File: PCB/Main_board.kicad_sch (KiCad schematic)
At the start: 296 parts, among them J1 USB_C_Receptacle_USB2.0_14P, J2 Conn_02x03_Odd_Even, SW1 SW_Push, SW10 SW_Push, SW11 SW_Push, SW12 SW_Push, SW13 SW_Push, SW14 SW_Push, SW15 SW_Push, SW16 SW_Push, SW17 SW_Push, SW18 SW_Push, SW19 SW_Push, SW2 SW_Push, SW20 SW_Push, SW21 SW_Push, SW22 SW_Push, SW23 SW_Push, SW24 SW_Push, SW25 SW_Push, SW26 SW_Push, SW27 SW_Push, SW28 SW_Push, SW29 SW_Push, SW3 SW_Push, SW30 SW_Push, SW31 SW_Push, SW32 SW_Push, SW33 SW_Push, SW34 SW_Push, SW35 SW_Push, SW36 SW_Push, SW37 SW_Push, SW38 SW_Push, SW39 SW_Push, SW4 SW_Push, SW40 SW_Push, SW41 SW_Push, SW42 SW_Push, SW43 SW_Push, SW44 SW_Push, SW45 SW_Push, SW46 SW_Push, SW47 SW_Push, SW48 SW_Push, SW49 SW_Push, SW5 SW_Push, SW50 SW_Push, SW51 SW_Push, SW52 SW_Push, SW53 SW_Push, SW54 SW_Push, SW55 SW_Push, SW56 SW_Push, SW57 SW_Push, SW58 SW_Push, SW59 SW_Push, SW6 SW_Push, SW60 SW_Push, SW61 SW_Push, SW62 SW_Push, SW63 SW_Push, SW64 SW_Push, SW65 SW_Push, SW66 SW_Push, SW67 SW_Push, SW68 SW_Push, SW69 SW_Push, SW7 SW_Push, SW70 SW_Push, SW71 SW_Push, SW72 SW_Push, SW73 SW_Push, SW74 SW_Push, SW75 SW_Push, SW76 SW_Push, SW77 SW_Push, SW78 SW_Push, SW79 SW_Push, SW8 SW_Push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

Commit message: Add: Production files
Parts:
- C1, C2, C3, C5: Comment C15850 -> (none); LCSC Part # (none) -> C15850; Link (none) -> https://jlcpcb.com/partdetail/C15850; Name (none) -> Capacitors; Unit Price ($) (none) -> 0.01
- C11: Comment C49678 -> (none); LCSC Part # (none) -> C49678; Link (none) -> https://jlcpcb.com/partdetail/C49678; Unit Price ($) (none) -> 0.01
- C4: Comment C28323 -> (none); LCSC Part # (none) -> C28323; Link (none) -> https://jlcpcb.com/partdetail/C28323; Unit Price ($) (none) -> 0.01
- C6: Comment C377773 -> (none); LCSC Part # (none) -> C377773; Link (none) -> https://jlcpcb.com/partdetail/C377773; Unit Price ($) (none) -> 0.02
- C7, C8: Comment C1779 -> (none); LCSC Part # (none) -> C1779; Link (none) -> https://jlcpcb.com/partdetail/C1779; Unit Price ($) (none) -> 0.01
- Conn1, Conn2, Conn3, Conn4: Link (none) -> https://www.aliexpress.com/item/1005007636554292.html; Name (none) -> 1X6 Magnetic Pogo Pins; Shipping (none) -> $4.65; Unit Price ($) (none) -> 1.84
- D1, D10, D11, D12, D13, D14, D15, D16, D17, D18, D19, D2, D20, D21, D22, D23, D24, D25, D26, D27, D28, D29, D3, D30, D31, D32, D33, D34, D35, D36, D37, D38, D39, D4, D40, D41, D42, D43, D44, D45, D46, D47, D48, D49, D5, D50, D51, D52, D53, D54, D55, D56, D57, D58, D59, D6, D60, D61, D62, D63, D64, D65, D66, D67, D68, D69, D7, D70, D71, D72, D73, D74, D75, D76, D77, D78, D79, D8, D80, D81, D82, D9: Comment C2099 -> (none); LCSC Part # (none) -> C2099; Link (none) -> https://jlcpcb.com/partdetail/C2099; Name (none) -> Diodes; Unit Price ($) (none) -> 0.01
- D104, D105, D106, D107, D108, D109, D110, D111, D112, D113, D114, D115, D116, D117, D118, D119, D120, D121, D122, D123, D124, D125, D126, D127, D128, D129, D130, D131, D132, D133, D134, D135, D136, D137, D138, D139, D140, D141, D142, D143, D144, D145, D146, D147, D148, D149, D150, D151, D152, D153, D154, D155, D156, D157, D158, D159, D160, D161, D162, D163, D164, D165, D166, D167, D168, D169, D170, D171, D172, D173, D174, D175, D176, D177, D178, D179, D180, D181, D182, D183, D184, D185: Comment C2890035 -> (none); LCSC Part # (none) -> C2890035; Link (none) -> https://jlcpcb.com/partdetail/C2890035; Name (none) -> SK6805 (LEDs); Unit Price ($) (none) -> 0.10
- D83: Comment C587142 -> (none); LCSC Part # (none) -> C587142; Link (none) -> https://jlcpcb.com/partdetail/C587142; Name (none) -> ESDA5V3L (ESD protector for I2C lines); Unit Price ($) (none) -> 0.04
- J1: Comment C165948 -> (none); LCSC Part # (none) -> C165948; Link (none) -> https://jlcpcb.com/partdetail/C165948; Name (none) -> USB Connector; Unit Price ($) (none) -> 0.18
- J2: Comment C6837603 -> (none); LCSC Part # (none) -> C6837603; Link (none) -> https://jlcpcb.com/partdetail/C6837603; Name (none) -> 2x3 1mm PinHeader (SWD Interface); Unit Price ($) (none) -> 0.03
- R1, R2: Comment C27834 -> (none); LCSC Part # (none) -> C27834; Link (none) -> https://jlcpcb.com/partdetail/C27834; Name (none) -> Resistors; Unit Price ($) (none) -> 0.01
- R10, R9: Comment C17673 -> (none); LCSC Part # (none) -> C17673; Link (none) -> https://jlcpcb.com/partdetail/C17673; Unit Price ($) (none) -> 0.01
- R11: Comment C17604 -> (none); LCSC Part # (none) -> C17604; Link (none) -> https://jlcpcb.com/partdetail/C17604; Unit Price ($) (none) -> 0.01
- R12, R6: Comment C2933502 -> (none); LCSC Part # (none) -> C2933502; Link (none) -> https://jlcpcb.com/partdetail/C2933502; Unit Price ($) (none) -> 0.01
- R13, R7: Comment C26112 -> (none); LCSC Part # (none) -> C26112; Link (none) -> https://jlcpcb.com/partdetail/C26112; Unit Price ($) (none) -> 0.01
- R19: Comment C17571 -> (none); LCSC Part # (none) -> C17571; Link (none) -> https://jlcpcb.com/partdetail/C17571; Unit Price ($) (none) -> 0.01
- R20, R22, R4: Comment C17414 -> (none); LCSC Part # (none) -> C17414; Link (none) -> https://jlcpcb.com/partdetail/C17414; Unit Price ($) (none) -> 0.01
- R21: Comment C4328 -> (none); LCSC Part # (none) -> C4328; Link (none) -> https://jlcpcb.com/partdetail/C4328; Unit Price ($) (none) -> 0.01
- R3: Comment C2933423 -> (none); LCSC Part # (none) -> C2933423; Link (none) -> https://jlcpcb.com/partdetail/C2933423; Unit Price ($) (none) -> 0.01
- R5, R8: Comment C17594 -> (none); LCSC Part # (none) -> C17594; Link (none) -> https://jlcpcb.com/partdetail/C17594; Unit Price ($) (none) -> 0.01
- SW1, SW10, SW11, SW12, SW13, SW14, SW15, SW16, SW17, SW18, SW19, SW2, SW20, SW21, SW22, SW23, SW24, SW25, SW26, SW27, SW28, SW29, SW3, SW30, SW31, SW32, SW33, SW34, SW35, SW36, SW37, SW38, SW39, SW4, SW40, SW41, SW42, SW43, SW44, SW45, SW46, SW47, SW48, SW49, SW5, SW50, SW51, SW52, SW53, SW54, SW55, SW56, SW57, SW58, SW59, SW6, SW60, SW61, SW62, SW63, SW64, SW65, SW66, SW67, SW68, SW69, SW7, SW70, SW71, SW72, SW73, SW74, SW75, SW76, SW77, SW78, SW79, SW8, SW80, SW81, SW82, SW9: Comment C5333465 -> (none); LCSC Part # (none) -> C5333465; Link (none) -> https://jlcpcb.com/partdetail/C5333465; Name (none) -> Keys; Unit Price ($) (none) -> 0.1213; moq (none) -> 73
- U1: Comment C687462 -> (none); LCSC Part # (none) -> C687462; Link (none) -> https://jlcpcb.com/partdetail/C687462; Name (none) -> LTC4217 (Hotswap-controller); Unit Price ($) (none) -> 11.90
- U11: Link (none) -> https://www.aliexpress.com/item/1005008597901992.html; Name (none) -> MT3608_Module (Boost converter/ 3V3 -> 5V); Shipping (none) -> $1.99; Unit Price ($) (none) -> 0.99
- U12: Comment C5167252 -> (none); LCSC Part # (none) -> C5167252; Link (none) -> https://jlcpcb.com/partdetail/C5167252; Name (none) -> Slide switch (1825232-1); Price None -> (none); Unit Price ($) (none) -> 0.84
- U2: Comment C283483 -> (none); LCSC Part # (none) -> C283483; Link (none) -> https://jlcpcb.com/partdetail/C283483; Name (none) -> USB6B1 (ESD protector for USB data lines); Unit Price ($) (none) -> 0.4702; moq (none) -> 19
- U3: Comment C5118826 -> (none); LCSC Part # (none) -> C5118826; Link (none) -> https://jlcpcb.com/partdetail/C5118826; Name (none) -> MDBT50Q-1MV2 (MCU); Unit Price ($) (none) -> 6.9468; moq (none) -> 2
- U4: Comment C95414 -> (none); LCSC Part # (none) -> C95414; Link (none) -> https://jlcpcb.com/partdetail/C95414; Name (none) -> LP2985-33DBVR (Voltage stabilizer/ 5V -> 3V3); Unit Price ($) (none) -> 0.12
- U5: Comment C424093 -> (none); LCSC Part # (none) -> C424093; Link (none) -> https://jlcpcb.com/partdetail/C424093; Name (none) -> MCP73831T-2ACI/OT; Unit Price ($) (none) -> 0.72

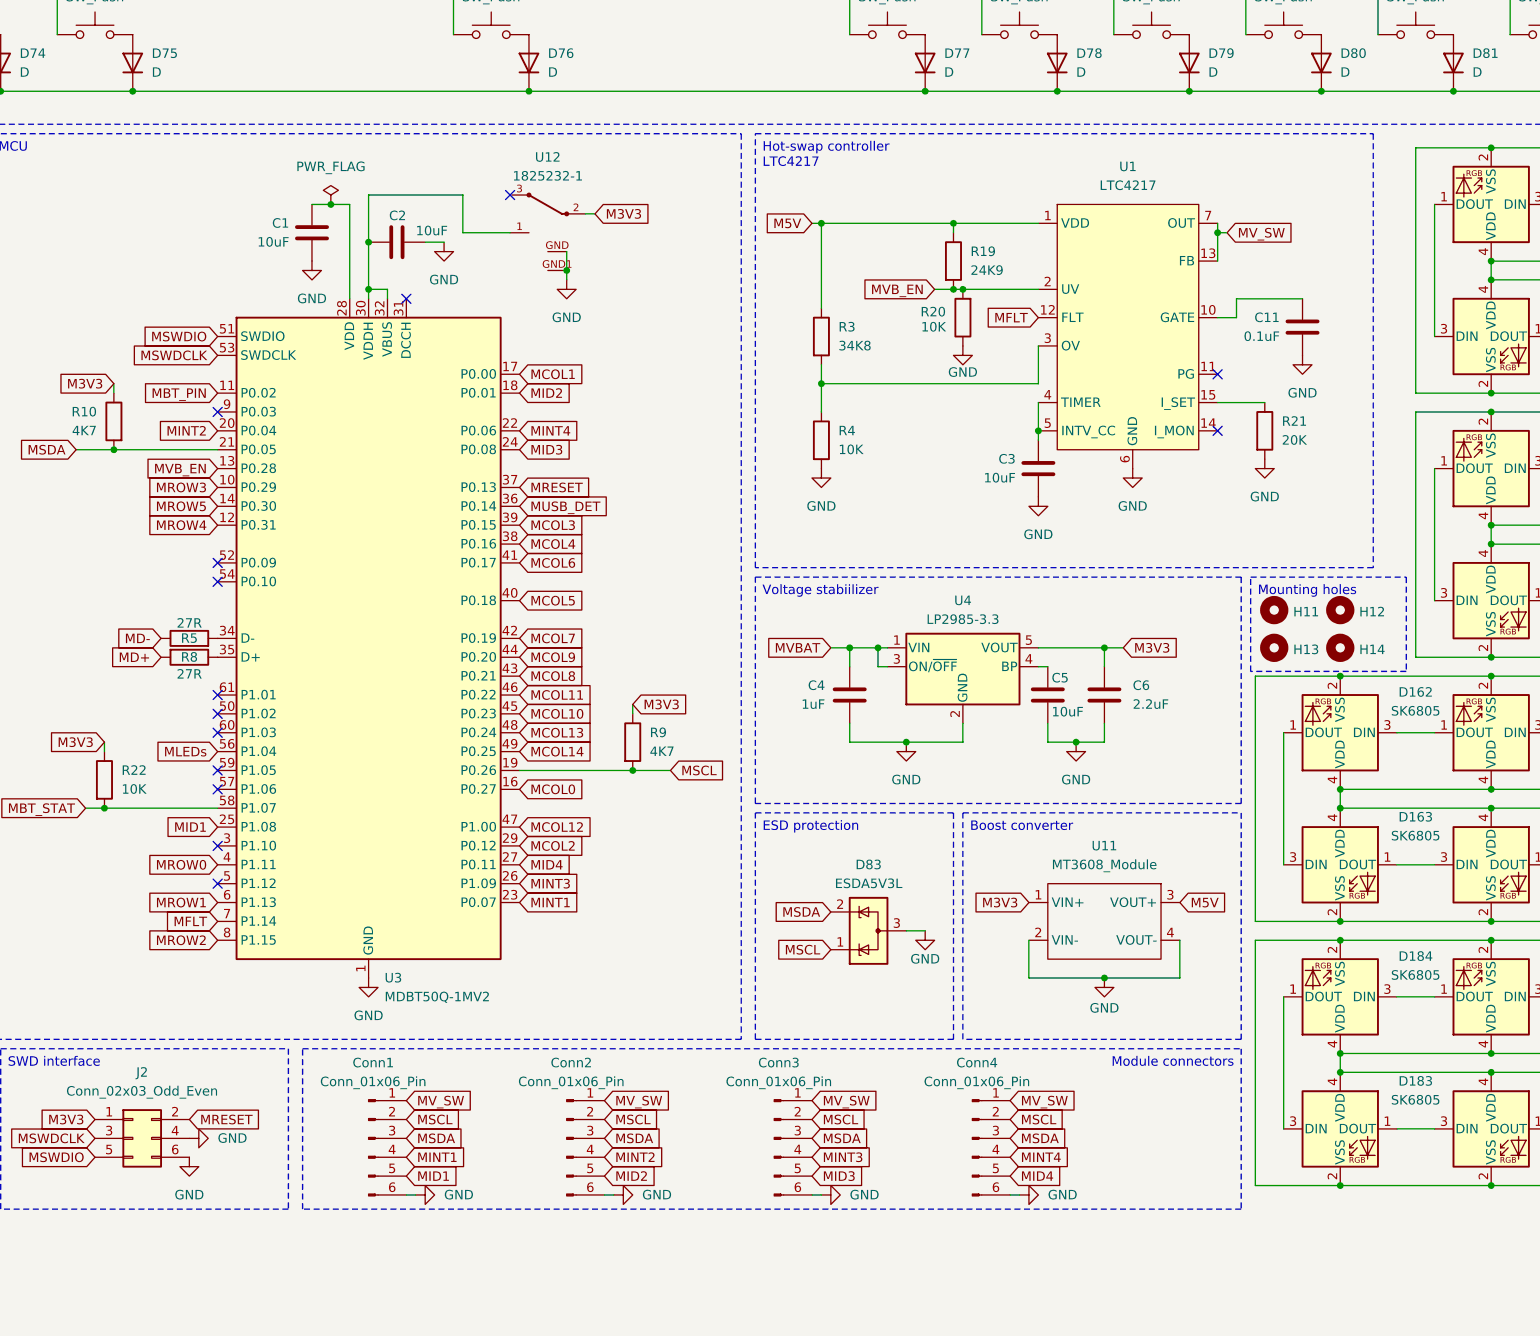
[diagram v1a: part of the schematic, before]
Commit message: Simplified design to reduce cost
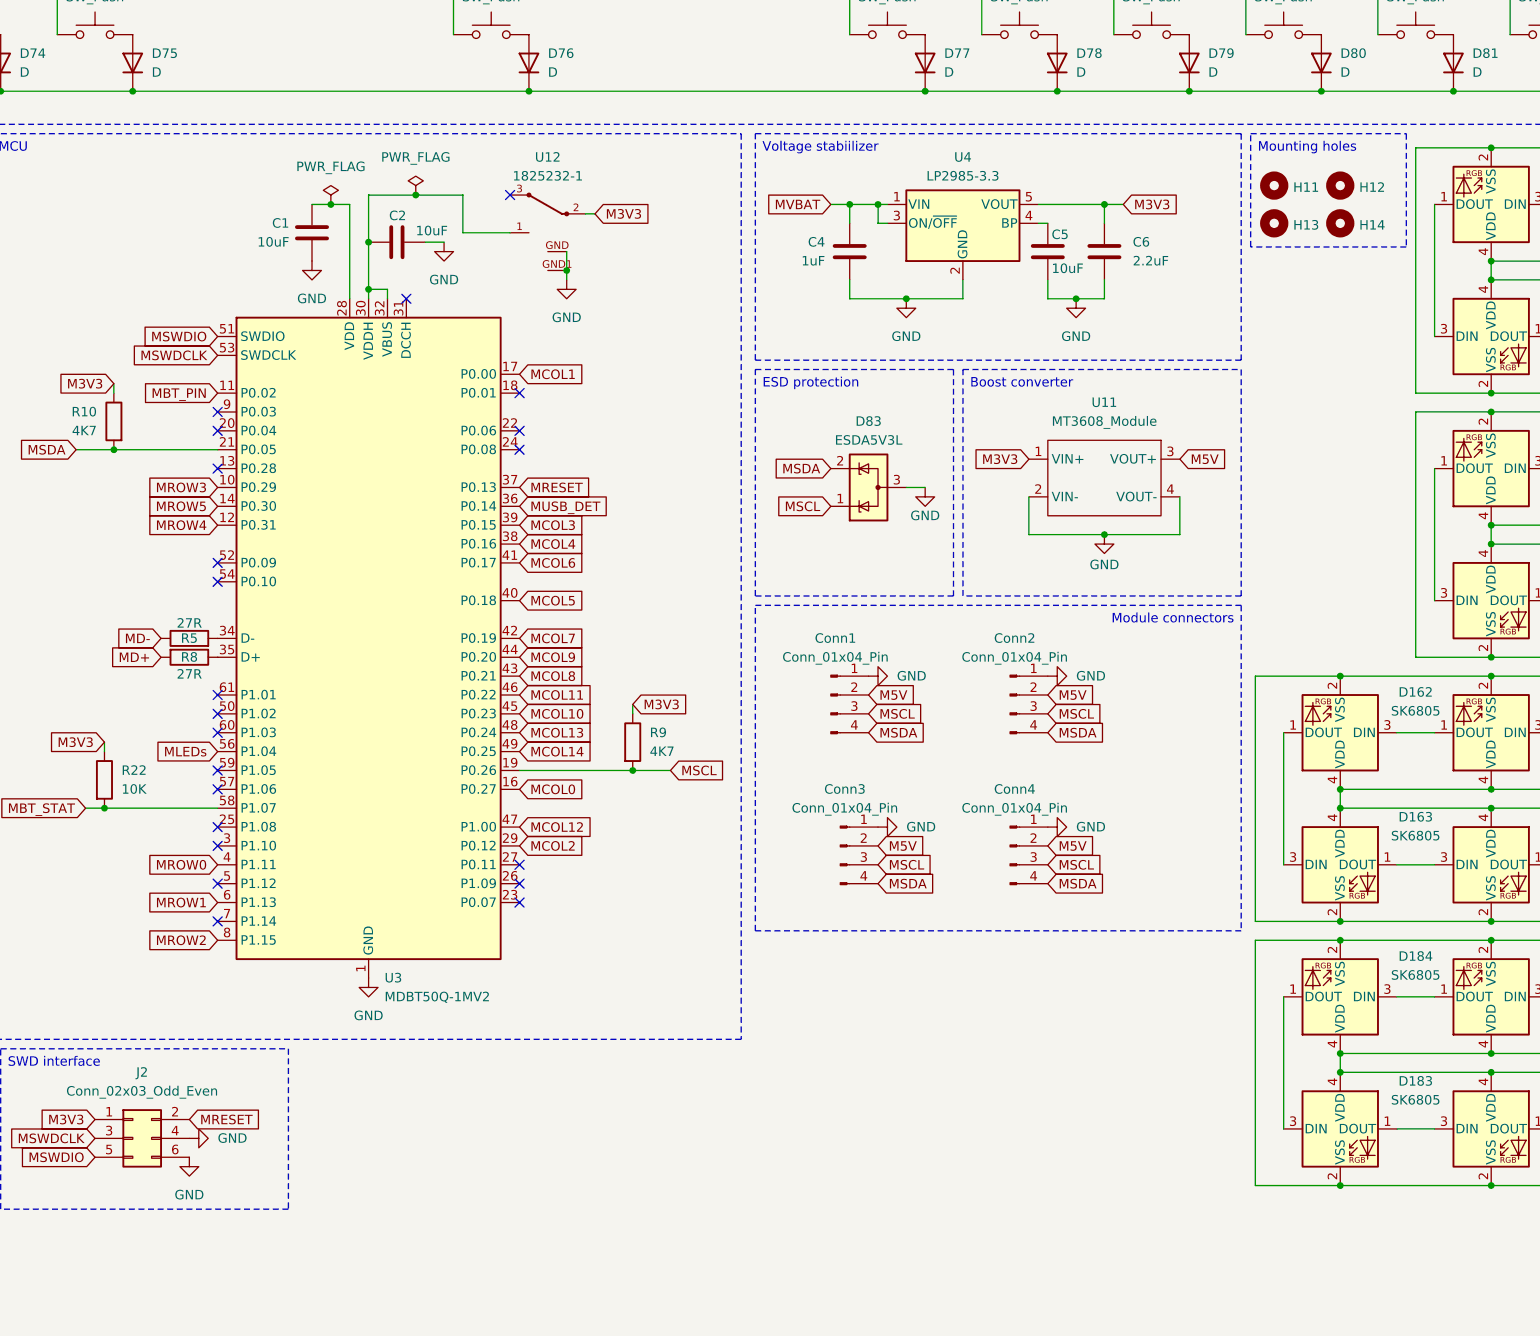
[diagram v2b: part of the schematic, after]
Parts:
- removed C11: 0.1uF, Capacitor_SMD:C_0805_2012Metric, symbol Device:C
- removed C3: 10uF, Capacitor_SMD:C_0805_2012Metric, symbol Device:C
- removed Conn1, Conn2, Conn3, Conn4: Conn_01x06_Pin, Connector_PinHeader_2.54mm:PinHeader_1x06_P2.54mm_Vertical, symbol Connector:Conn_01x06_Pin
- removed R19: 24K9, Resistor_SMD:R_0805_2012Metric, symbol Device:R
- removed R20, R4: 10K, Resistor_SMD:R_0805_2012Metric, symbol Device:R
- removed R21: 20K, Resistor_SMD:R_0805_2012Metric, symbol Device:R
- removed R3: 34K8, Resistor_SMD:R_0805_2012Metric, symbol Device:R
- removed U1: LTC4217, DFN-16_DHC_LIT:DFN-16_DHC_LIT, symbol Custom Symbols:LTC4217
- added Conn1, Conn2, Conn3, Conn4: Conn_01x04_Pin, Connector_PinHeader_2.54mm:PinHeader_1x04_P2.54mm_Vertical, symbol Connector:Pogopin_connector_01x04
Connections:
- net GND: now also Conn1.1 (Pin_1), Conn2.1 (Pin_1), Conn3.1 (Pin_1), Conn4.1 (Pin_1)
- net MSCL: now also Conn1.3 (Pin_3), Conn2.3 (Pin_3), Conn3.3 (Pin_3), Conn4.3 (Pin_3)
- net MSDA: now also Conn1.4 (Pin_4), Conn2.4 (Pin_4), Conn3.4 (Pin_4), Conn4.4 (Pin_4)
- net MFLT: no longer names the net of U3.7 (P1.14)
- net MID1: no longer names the net of U3.25 (P1.08)
- net MID2: no longer names the net of U3.18 (P0.01)
- net MID3: no longer names the net of U3.24 (P0.08)
- net MID4: no longer names the net of U3.27 (P0.11)
- net MINT1: no longer names the net of U3.23 (P0.07)
- net MINT2: no longer names the net of U3.20 (P0.04)
- net MINT3: no longer names the net of U3.26 (P1.09)
- net MINT4: no longer names the net of U3.22 (P0.06)
- net MVB_EN: no longer names the net of U3.13 (P0.28)
- net VDD renamed M5V
- net M5V: now also Conn1.2 (Pin_2), Conn2.2 (Pin_2), Conn3.2 (Pin_2), Conn4.2 (Pin_2)
- no-connect marks 15 -> 23
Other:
- moved on the sheet: C4, C5, C6, D83, H11, H12, H13, H14, U11, U4

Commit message: Update: Schematic and mainboard PCB
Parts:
- removed C4: 1uF, Capacitor_SMD:C_0805_2012Metric, symbol Device:C
- removed C5: 10uF, Capacitor_SMD:C_0805_2012Metric, symbol Device:C
- removed C6: 2.2uF, Capacitor_SMD:C_0805_2012Metric, symbol Device:C
- removed D104, D105, D106, D107, D108, D109, D110, D111, D112, D113, D114, D115, D116, D117, D118, D119, D120, D121, D122, D123, D124, D125, D126, D127, D128, D129, D130, D131, D132, D133, D134, D135, D136, D137, D138, D139, D140, D141, D142, D143, D144, D145, D146, D147, D148, D149, D150, D151, D152, D153, D154, D155, D156, D157, D158, D159, D160, D161, D162, D163, D164, D165, D166, D167, D168, D169, D170, D171, D172, D173, D174, D175, D176, D177, D178, D179, D180, D181, D182, D183, D184, D185: SK6805, LED_SMD:LED_SK6805_PLCC4_2.4x2.7mm_P1.3mm, symbol LED:SK6805
- removed U11: MT3608_Module, MT3608-Module:MT3608-Module, symbol Custom Symbols:MT3608_Module
- removed U4: LP2985-3.3, Package_TO_SOT_SMD:SOT-23-5, symbol Regulator_Linear:LP2985-3.3
- added C1, C3: 10uF, Capacitor_SMD:C_0805_2012Metric, symbol Device:C
- added L1: 10uH, Inductor_SMD:L_0805_2012Metric, symbol Device:L
- added Q1, Q2, Q3: Q_PMOS_GSD, Package_TO_SOT_SMD:SOT-23, symbol Transistor_FET:Q_PMOS_GSD
- added R1: 2K, Resistor_SMD:R_0805_2012Metric, symbol Device:R
- added R13: 27R, Resistor_SMD:R_0805_2012Metric, symbol Device:R
- added R3, R5, R6: 806K, Resistor_SMD:R_0805_2012Metric, symbol Device:R
- SW1, SW10, SW11, SW12, SW13, SW14, SW15, SW16, SW17, SW18, SW19, SW2, SW20, SW21, SW22, SW23, SW24, SW25, SW26, SW27, SW29, SW3, SW31, SW32, SW33, SW34, SW35, SW36, SW37, SW38, SW39, SW4, SW40, SW41, SW42, SW44, SW46, SW47, SW48, SW49, SW5, SW50, SW51, SW52, SW53, SW54, SW55, SW56, SW58, SW6, SW60, SW61, SW62, SW63, SW64, SW65, SW66, SW67, SW68, SW69, SW7, SW71, SW72, SW73, SW74, SW75, SW77, SW78, SW79, SW8, SW80, SW81, SW82, SW9: footprint PCM_marbastlib-choc:SW_choc_v1_HS_CPG135001S30_1u -> Footprints:Kailh_choc_HS_V2_1u
- SW28: footprint PCM_marbastlib-choc:SW_choc_v1_HS_CPG135001S30_1.75u -> Footprints:Kailh_choc_HS_V2_2u
- SW30, SW43: footprint PCM_marbastlib-choc:SW_choc_v1_HS_CPG135001S30_1.5u -> Footprints:Kailh_choc_HS_V2_1.5u
- SW45, SW70: footprint PCM_marbastlib-choc:SW_choc_v1_HS_CPG135001S30_1.75u -> Footprints:Kailh_choc_HS_V2_1.75u
- SW57, SW59: footprint PCM_marbastlib-choc:SW_choc_v1_HS_CPG135001S30_2.25u -> Footprints:Kailh_choc_HS_V2_2.25u
- SW76: footprint PCM_marbastlib-choc:SW_choc_v1_HS_CPG135001S30_2.25u -> Footprints:Kailh_choc_HS_V2_6u
- renumbered C1 to C4, C7 to C5, C8 to C6, D83 to ESD1, H11 to H1, H12 to H2, H15 to H3, H16 to H4, H17 to H5, H18 to H6, H13 to H7, H14 to H8, R7 to R10, R8 to R11, R9 to R12, R22 to R14, R11 to R15, R12 to R16, R13 to R17, R1 to R2, R2 to R4, R10 to R7, R5 to R8, R6 to R9, U12 to U1, U5 to U4
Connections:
- net M5V is gone; now on net MVSYS: Conn1.2 (Pin_2), Conn2.2 (Pin_2), Conn3.2 (Pin_2), Conn4.2 (Pin_2)
- net GND: now also C4.1, J2.3 (Pin_3), J2.5 (Pin_5), U1.2, C1.2, C3.2, R3.2; no longer C4.2, J2.4 (Pin_4), J2.6 (Pin_6)
- net M3V3: now also C4.2, U3.28 (VDD), L1.1; no longer U1.2
- net MBT_PIN: now also U3.57 (P1.06); no longer U3.11 (P0.02)
- net MCOL10: now also U3.37 (P0.13); no longer U3.45 (P0.23)
- net MCOL11: now also U3.38 (P0.16); no longer U3.46 (P0.22)
- net MCOL12: now also U3.39 (P0.15); no longer U3.47 (P1.00)
- net MCOL13: now also U3.40 (P0.18); no longer U3.48 (P0.24)
- net MCOL14: now also U3.41 (P0.17); no longer U3.49 (P0.25)
- net MCOL2: now also U3.18 (P0.01); no longer U3.29 (P0.12)
- net MCOL3: now also U3.23 (P0.07); no longer U3.39 (P0.15)
- net MCOL4: now also U3.24 (P0.08); no longer U3.38 (P0.16)
- net MCOL5: now also U3.25 (P1.08); no longer U3.40 (P0.18)
- net MCOL6: now also U3.26 (P1.09); no longer U3.41 (P0.17)
- net MCOL7: now also U3.27 (P0.11); no longer U3.42 (P0.19)
- net MCOL8: now also U3.29 (P0.12); no longer U3.43 (P0.21)
- net MCOL9: now also U3.36 (P0.14); no longer U3.44 (P0.20)
- net MLEDs: now also R13.1; no longer U3.56 (P1.04)
- net MRESET: now also U3.50 (P1.02); no longer U3.37 (P0.13)
- net MSCL: now also Conn1.4 (Pin_4), Conn2.4 (Pin_4), Conn3.4 (Pin_4), Conn4.4 (Pin_4), U3.22 (P0.06); no longer Conn1.3 (Pin_3), Conn2.3 (Pin_3), Conn3.3 (Pin_3), Conn4.3 (Pin_3), U3.19 (P0.26)
- net MSDA: now also Conn1.3 (Pin_3), Conn2.3 (Pin_3), Conn3.3 (Pin_3), Conn4.3 (Pin_3), U3.20 (P0.04); no longer Conn1.4 (Pin_4), Conn2.4 (Pin_4), Conn3.4 (Pin_4), Conn4.4 (Pin_4), U3.21 (P0.05)
- net MSWDCLK: now also J2.6 (Pin_6); no longer J2.3 (Pin_3)
- net MSWDIO: now also J2.4 (Pin_4); no longer J2.5 (Pin_5)
- net MUSB_DET: no longer U3.36 (P0.14)
- net MVBAT: now also Q1.2 (S)
- net MVBUS: now also U3.32 (VBUS), C3.1, Q1.1 (G), R3.1
- net MVSYS: now reaches C2.1, U3.30 (VDDH)
- net MVSYS: now also C1.1, Q2.2 (S), Q3.3 (D), R5.2; no longer U1.1, U3.32 (VBUS)
- net D+: now reaches R11.1, U3.35 (D+)
- net D-: now reaches R8.2, U3.34 (D-)
- net at U3.31 (DCCH): now also L1.2
- net MLED_Enable: now reaches U3.59 (P1.05)
- net MLED_Enable: now also R1.1
- new net: Q2.1 (G), R1.2, R5.1
- new net: R13.2, U3.56 (P1.04)
- new net: Q3.1 (G), R6.1, U1.1
- new net M5V_LED: Q2.3 (D)
- new net MV_WT: Q1.3 (D), Q3.2 (S), R6.2
- no-connect marks 23 -> 10
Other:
- added sheet MLEDs (MLEDs.kicad_sch)
- moved on the sheet: C2, C4, Conn1, Conn2, Conn3, Conn4, ESD1, H1, H2, H3, H4, H5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
